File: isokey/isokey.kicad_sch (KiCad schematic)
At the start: 69 parts, among them J1 PadExp Left, J2 PadExp Right, Q1 BSS138, SW73 RotaryEncoder_Switch, SW74 RotaryEncoder_Switch, U1 BlackPill_STLINK, U4 TLV73318PDBV

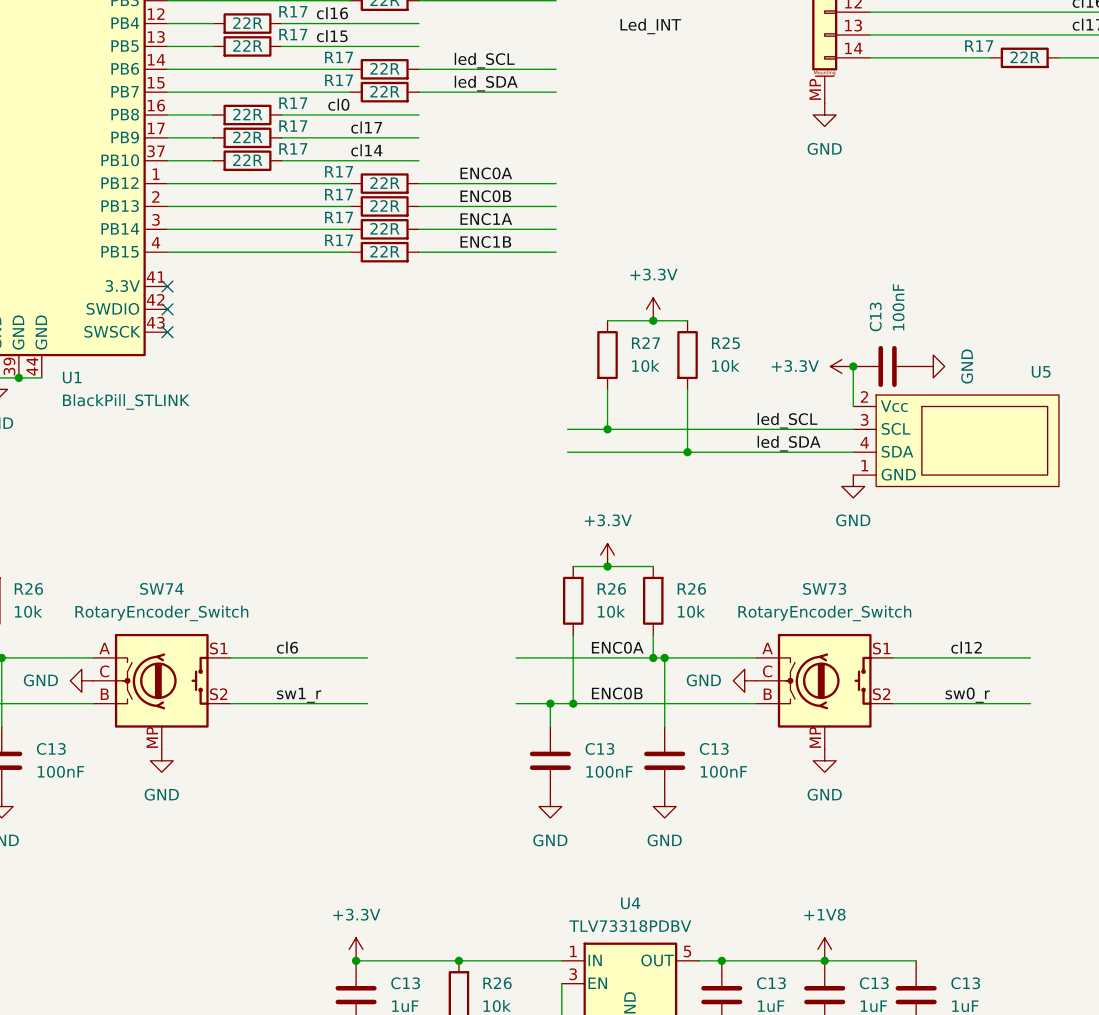
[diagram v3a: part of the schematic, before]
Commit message: add ir sensor for trackball
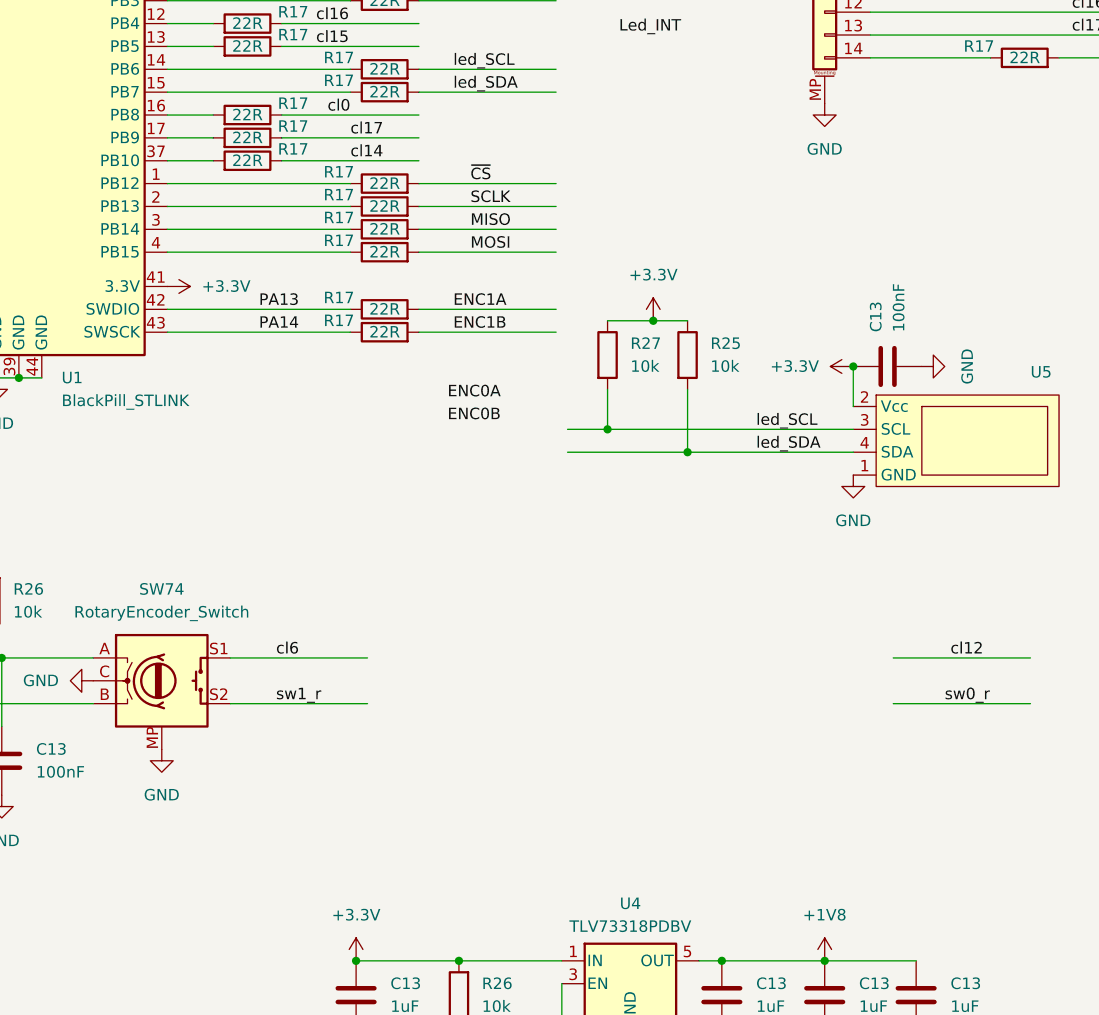
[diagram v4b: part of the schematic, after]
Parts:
- removed C13 (x2): 100nF, Capacitor_SMD:C_0603_1608Metric_Pad1.08x0.95mm_HandSolder, symbol Device:C
- removed R26 (x2): 10k, Resistor_SMD:R_0603_1608Metric_Pad0.98x0.95mm_HandSolder, symbol Device:R
- removed SW73: RotaryEncoder_Switch, Rotary_Encoder:RotaryEncoder_Alps_EC12E-Switch_Vertical_H20mm_CircularMountingHoles, symbol Device:RotaryEncoder_Switch
- added R17 (x2): 22R, Resistor_SMD:R_0603_1608Metric_Pad0.98x0.95mm_HandSolder, symbol Device:R
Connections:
- net +3.3V: now also U1.41 (3.3V)
- net ENC0A: no longer R17.2
- net ENC0B: no longer R17.2
- net ENC1A: now also R17.2; no longer R17.2
- net ENC1B: now also R17.2; no longer R17.2
- net MISO: now also R17.2
- net MOSI: now also R17.2
- net SCLK: now also R17.2
- net ~{CS}: now also R17.2
- net PA13: now reaches U1.42 (SWDIO)
- net PA13: now also R17.1
- net PA14: now reaches U1.43 (SWSCK)
- net PA14: now also R17.1
- no-connect marks 6 -> 3

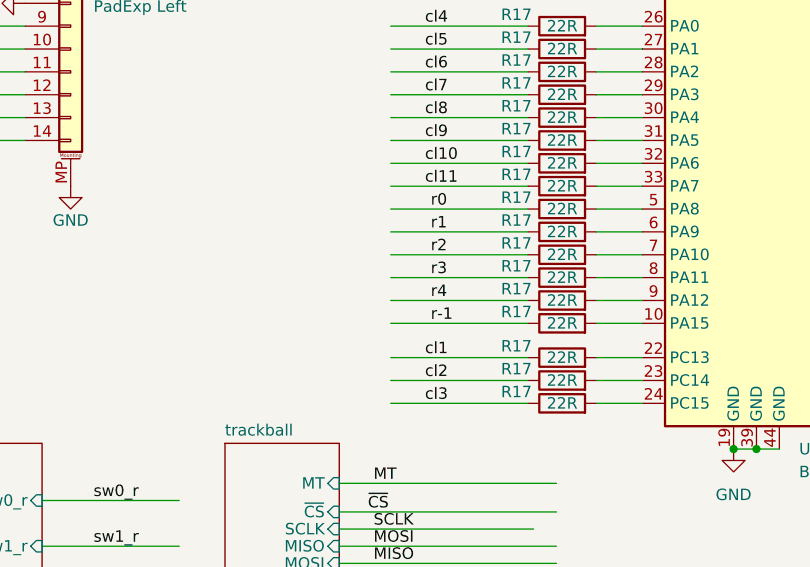
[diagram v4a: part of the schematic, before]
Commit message: Add trackball routing
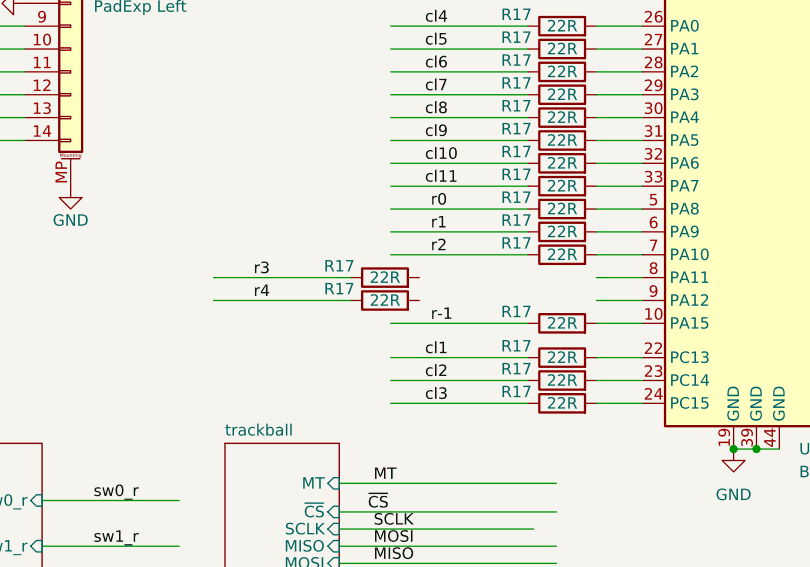
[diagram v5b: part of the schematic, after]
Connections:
- net at R17.2: no longer U1.9 (PA12)
- net at R17.2: no longer U1.8 (PA11)
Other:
- moved on the sheet: R17
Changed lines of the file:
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@@
     (stroke (width 0) (type default))
   )
-  (wire (pts (xy 102.87 68.58) (xy 118.11 68.58))
+  (wire (pts (xy 83.185 68.58) (xy 98.425 68.58))
     (stroke (width 0) (type default))
   )
@@
     (stroke (width 0) (type default))
   )
-  (wire (pts (xy 102.87 66.04) (xy 118.11 66.04))
+  (wire (pts (xy 83.185 66.04) (xy 98.425 66.04))
     (stroke (width 0) (type default))
   )
@@
     (effects (font (size 1.27 1.27)) (justify left bottom))
   )
-  (label "r3" (at 107.315 66.04 0) (fields_autoplaced)
+  (label "r3" (at 87.63 66.04 0) (fields_autoplaced)
     (effects (font (size 1.27 1.27)) (justify left bottom))
   )
@@
     (effects (font (size 1.27 1.27)) (justify left bottom))
   )
-  (label "r4" (at 107.315 68.58 0) (fields_autoplaced)
+  (label "r4" (at 87.63 68.58 0) (fields_autoplaced)
     (effects (font (size 1.27 1.27)) (justify left bottom))
   )
@@
     )
   )
-  (symbol (lib_id "Device:R") (at 121.92 68.58 90) (unit 1)
-    (in_bom yes) (on_board yes) (dnp no)
-    (property "Reference" "R17" (at 116.84 67.31 90)
-      (effects (font (size 1.27 1.27)))
-    )
-    (property "Value" "22R" (at 121.92 68.58 90)
-      (effects (font (size 1.27 1.27)))
-    )
-    (property "Footprint" "Resistor_SMD:R_0603_1608Metric_Pad0.98x0.95mm_HandSolder" (at 121.92 70.358 90)
-      (effects (font (size 1.27 1.27)) hide)
-    )
-    (property "Datasheet" "~" (at 121.92 68.58 0)
+  (symbol (lib_id "Device:R") (at 102.235 68.58 90) (unit 1)
+    (in_bom yes) (on_board yes) (dnp no)
+    (property "Reference" "R17" (at 97.155 67.31 90)
+      (effects (font (size 1.27 1.27)))
+    )
+    (property "Value" "22R" (at 102.235 68.58 90)
+      (effects (font (size 1.27 1.27)))
+    )
+    (property "Footprint" "Resistor_SMD:R_0603_1608Metric_Pad0.98x0.95mm_HandSolder" (at 102.235 70.358 90)
+      (effects (font (size 1.27 1.27)) hide)
+    )
+    (property "Datasheet" "~" (at 102.235 68.58 0)
       (effects (font (size 1.27 1.27)) hide)
     )
@@
     )
   )
-  (symbol (lib_id "Device:R") (at 121.92 66.04 90) (unit 1)
-    (in_bom yes) (on_board yes) (dnp no)
-    (property "Reference" "R17" (at 116.84 64.77 90)
-      (effects (font (size 1.27 1.27)))
-    )
-    (property "Value" "22R" (at 121.92 66.04 90)
-      (effects (font (size 1.27 1.27)))
-    )
-    (property "Footprint" "Resistor_SMD:R_0603_1608Metric_Pad0.98x0.95mm_HandSolder" (at 121.92 67.818 90)
-      (effects (font (size 1.27 1.27)) hide)
-    )
-    (property "Datasheet" "~" (at 121.92 66.04 0)
-      (effects (font (size 1.27 1.27)) hide)
-    )
+  (symbol (lib_id "Device:R") (at 102.235 66.04 90) (unit 1)
+    (in_bom yes) (on_board yes) (dnp no)
+    (property "Reference" "R17" (at 97.155 64.77 90)
+      (effects (font (size 1.27 1.27)))
+    )
+    (property "Value" "22R" (at 102.235 66.04 90)
+      (effects (font (size 1.27 1.27)))
+    )
+    (property "Footprint" "Resistor_SMD:R_0603_1608Metric_Pad0.98x0.95mm_HandSolder" (at 102.235 67.818 90)
+      (effects (font (size 1.27 1.27)) hide)
+    )
+    (property "Datasheet" "~" (at 102.235 66.04 0)
+      (effects (font (size 1.27 1.27)) hide)
+    )

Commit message: isokey: start splitting
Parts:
- renumbered J2 to J1, J1 to J2, SW74 to RSW1, U5 to U2, U4 to U3
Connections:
- net at R17.2: now also U1.9 (PA12)
- net at R17.2: now also U1.8 (PA11)
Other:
- removed sheet trackball
- sheet keyplate ports: added none; removed cl10, cl11, cl12, cl13, cl14, cl15, r-1
- moved on the sheet: R17

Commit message: Continue routing
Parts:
- U1: footprint Module:BlackPill -> Module:BlackPill_doble_top-bot
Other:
- moved on the sheet: C13, Q1, R17, R25, R26, R27, RSW1, U1, U2, U3

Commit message: Continue routing
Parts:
- removed J1: PadExp Right, Connector_JST:JST_GH_SM14B-GHS-TB_1x14-1MP_P1.25mm_Horizontal, symbol Connector_Generic_MountingPin:Conn_01x14_MountingPin
- removed J2: PadExp Left, Connector_JST:JST_GH_SM14B-GHS-TB_1x14-1MP_P1.25mm_Horizontal, symbol Connector_Generic_MountingPin:Conn_01x14_MountingPin
- added TP1: CL6, TestPoint:Testpoint_Pad_1.0x2.0mm, symbol Connector:TestPoint
- added TP10, TP6: GND, TestPoint:Testpoint_Pad_1.0x2.0mm, symbol Connector:TestPoint
- added TP11: W1, TestPoint:Testpoint_Pad_1.0x2.0mm, symbol Connector:TestPoint
- added TP2: CL7, TestPoint:Testpoint_Pad_1.0x2.0mm, symbol Connector:TestPoint
- added TP3: CL8, TestPoint:Testpoint_Pad_1.0x2.0mm, symbol Connector:TestPoint
- added TP4: CL9, TestPoint:Testpoint_Pad_1.0x2.0mm, symbol Connector:TestPoint
- added TP5, TP9: +5V, TestPoint:Testpoint_Pad_1.0x2.0mm, symbol Connector:TestPoint
- added TP7: CL10, TestPoint:Testpoint_Pad_1.0x2.0mm, symbol Connector:TestPoint
- added TP8: ID, TestPoint:Testpoint_Pad_1.0x2.0mm, symbol Connector:TestPoint
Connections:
- net MISO is gone; now on net cl2: R17.2
- net MOSI is gone; now on net cl1: R17.2
- net SCLK is gone; now on net cl3: R17.2
- net ~{CS} is gone; now on net cl4: R17.2
- net +5V: now also TP5.1, TP9.1
- net GND: now also TP10.1, TP6.1
- net cl1: no longer R17.1
- net cl10: now also TP7.1; no longer R17.1
- net cl11: no longer R17.1
- net cl2: no longer R17.1
- net cl3: no longer R17.1
- net cl4: no longer R17.1
- net cl5: no longer R17.1
- net cl6: now also TP1.1; no longer R17.1
- net cl7: now also TP2.1; no longer R17.1
- net cl8: now also TP3.1; no longer R17.1
- net cl9: now also TP4.1; no longer R17.1
- net led_w1_out: now also R17.2
- net port_id: no longer R17.2
- net r-1: no longer R17.1
- net r0: no longer R17.1
- net r1: no longer R17.1
- net r2: no longer R17.1
- net r3: no longer R17.1
- net r4: no longer R17.1
- net at R17.1: now also TP8.1
- net at R17.1: now also TP11.1
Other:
- moved on the sheet: H1, H2, H3, H4, R17
